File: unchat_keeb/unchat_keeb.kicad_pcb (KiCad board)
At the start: 2 copper layers, 245 parts, among them U1 74HC365, U10 74HC14, U11 74HC14, U12 74HC14, U13 74HC174, U14 74HC174, U15 74HC174, U16 74HC174, U17 74HC174, U18 74HC174, U19 74HC365, U2 74HC365, U20 74HC365, U21 74HC365, U22 74HC365, U23 74HC365, U24 74HC365, U3 74HC365, U4 74HC365, U5 74HC365, U6 74HC365, U7 74HC14, U8 74HC14, U9 74HC14, U99 Raspberry_Pi_Pico

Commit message: Add extra columns, updating to 42-key design
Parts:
- added C37: 0.1uF, Capacitor_SMD:C_0805_2012Metric, F.Cu at (142.8, 142.2)
- added C38: 0.1uF, Capacitor_SMD:C_0805_2012Metric, F.Cu at (142.8, 145.2)
- added C39: 0.1uF, Capacitor_SMD:C_0805_2012Metric, F.Cu at (142.8, 148.2)
- added C40: 0.1uF, Capacitor_SMD:C_0805_2012Metric, F.Cu at (142.8, 151.2)
- added C41: 0.1uF, Capacitor_SMD:C_0805_2012Metric, F.Cu at (142.8, 154.2)
- added C42: 0.1uF, Capacitor_SMD:C_0805_2012Metric, F.Cu at (142.8, 157.2)
- added L1: LED, LED_SMD:LED_0603_1608Metric, F.Cu at (23.7, 133.8)
- added L13: LED, LED_SMD:LED_0603_1608Metric, F.Cu at (23.7, 139.0)
- added L22: LED, LED_SMD:LED_0603_1608Metric, F.Cu at (342.1, 68.9)
- added L28: LED, LED_SMD:LED_0603_1608Metric, F.Cu at (342.1, 71.5)
- added L34: LED, LED_SMD:LED_0603_1608Metric, F.Cu at (342.1, 74.1)
- added L7: LED, LED_SMD:LED_0603_1608Metric, F.Cu at (23.7, 136.4)
- added R103: 100, Resistor_SMD:R_0805_2012Metric, F.Cu at (342.3, 66.1)
- added R117: 68k, Resistor_SMD:R_0805_2012Metric, F.Cu at (147.3, 142.2)
- added R118: 68k, Resistor_SMD:R_0805_2012Metric, F.Cu at (147.3, 145.1)
- added R119: 68k, Resistor_SMD:R_0805_2012Metric, F.Cu at (147.3, 148.1)
- added R120: 68k, Resistor_SMD:R_0805_2012Metric, F.Cu at (147.3, 151.0)
- added R121: 68k, Resistor_SMD:R_0805_2012Metric, F.Cu at (151.7, 142.2)
- added R122: 68k, Resistor_SMD:R_0805_2012Metric, F.Cu at (151.7, 145.1)
- added R123: 1k, Resistor_SMD:R_0805_2012Metric, F.Cu at (151.7, 148.1)
- added R124: 1k, Resistor_SMD:R_0805_2012Metric, F.Cu at (151.7, 151.0)
- added R125: 1k, Resistor_SMD:R_0805_2012Metric, F.Cu at (156.1, 142.2)
- added R126: 1k, Resistor_SMD:R_0805_2012Metric, F.Cu at (156.1, 145.1)
- added R127: 1k, Resistor_SMD:R_0805_2012Metric, F.Cu at (156.1, 148.1)
- added R128: 1k, Resistor_SMD:R_0805_2012Metric, F.Cu at (156.1, 151.0)
- added R73: 100, Resistor_SMD:R_0805_2012Metric, F.Cu at (19.5, 134.0)
- added R79: 100, Resistor_SMD:R_0805_2012Metric, F.Cu at (19.5, 136.9)
- added R85: 100, Resistor_SMD:R_0805_2012Metric, F.Cu at (19.5, 139.9)
- added R91: 100, Resistor_SMD:R_0805_2012Metric, F.Cu at (342.3, 60.2)
- added R97: 100, Resistor_SMD:R_0805_2012Metric, F.Cu at (342.3, 63.2)
- added S1: Keyswitch, GKanwarLibrary:Choc_V1_LED_1.00u, F.Cu at (23.0, 81.3)
- added S13: Keyswitch, GKanwarLibrary:Choc_V1_LED_1.00u, F.Cu at (23.0, 117.5)
- added S22: Keyswitch, GKanwarLibrary:Choc_V1_LED_1.00u, F.Cu at (330.5, 67.8)
- added S28: Keyswitch, GKanwarLibrary:Choc_V1_LED_1.00u, F.Cu at (330.5, 85.9)
- added S34: Keyswitch, GKanwarLibrary:Choc_V1_LED_1.00u, F.Cu at (330.5, 104.0)
- added S7: Keyswitch, GKanwarLibrary:Choc_V1_LED_1.00u, F.Cu at (23.0, 99.4)
- added U25: 74HC14, Package_SO:TSSOP-14_4.4x5mm_P0.65mm, F.Cu at (149.4, 155.8)
- added U26: 74HC174, Package_SO:TSSOP-16_4.4x5mm_P0.65mm, F.Cu at (151.1, 171.6)
- added U27: 74HC365, Package_SO:TSSOP-16_4.4x5mm_P0.65mm, F.Cu at (151.1, 178.2)
- added U66: 74HC365, Package_SO:TSSOP-16_4.4x5mm_P0.65mm, F.Cu at (167.6, 156.2)
- renumbered L8 to L10, L9 to L11, L10 to L12, L11 to L14, L12 to L15, L13 to L16, L14 to L17, L15 to L18, L16 to L19, L1 to L2, L17 to L20, L18 to L21, L19 to L23, L20 to L24, L21 to L25, L22 to L26, L23 to L27, L24 to L29, L2 to L3, L25 to L30, L26 to L31, L27 to L32, L28 to L33, L29 to L35, L30 to L36, L31 to L39, L3 to L4, L32 to L40, L33 to L41, L34 to L42, L35 to L43, L36 to L44, L4 to L5, L5 to L6, L6 to L8, L7 to L9, R98 to R100, R95 to R101, R92 to R102, R107 to R104, R103 to R105, R99 to R106, R96 to R107, R93 to R108, R88 to R111, R89 to R112, R90 to R113, R108 to R114, R104 to R115, R100 to R116, R73 to R74, R74 to R75, R75 to R76, R76 to R77, R77 to R78, R78 to R80, R79 to R81, R80 to R82, R81 to R83, R82 to R84, R83 to R86, R84 to R87, R85 to R88, R86 to R89, R87 to R90, R105 to R92, R101 to R93, R97 to R94, R94 to R95, R91 to R96, R106 to R98, R102 to R99, S8 to S10, S9 to S11, S10 to S12, S11 to S14, S12 to S15, S13 to S16, S14 to S17, S15 to S18, S16 to S19, S1 to S2, S17 to S20, S18 to S21, S19 to S23, S20 to S24, S21 to S25, S22 to S26, S23 to S27, S24 to S29, S2 to S3, S25 to S30, S26 to S31, S27 to S32, S28 to S33, S29 to S35, S30 to S36, S31 to S37, S32 to S38, S33 to S39, S3 to S4, S34 to S40, S35 to S41, S36 to S42, S4 to S5, S5 to S6, S6 to S8, S7 to S9
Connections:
- net /T1 renamed /Left Debounce 1-6/BF6
- net /T10 renamed /Left Debounce 7-12/BF3
- net /T11 renamed /Left Debounce 7-12/BF2
- net /T12 renamed /Left Debounce 7-12/BF1
- net /T13 renamed /Left Debounce 13-18/BF6
- net /T14 renamed /Left Debounce 13-18/BF5
- net /T15 renamed /Left Debounce 13-18/BF4
- net /T16 renamed /Left Debounce 13-18/BF3
- net /T17 renamed /Left Debounce 13-18/BF2
- net /T18 renamed /Left Debounce 13-18/BF1
- net /T19 renamed /Right Debounce 1-7/BF6
- net /T2 renamed /Left Debounce 1-6/BF5
- net /T20 renamed /Right Debounce 1-7/BF5
- net /T21 renamed /Right Debounce 1-7/BF4
- net /T22 renamed /Right Debounce 1-7/BF3
- net /T23 renamed /Right Debounce 1-7/BF2
- net /T24 renamed /Right Debounce 1-7/BF1
- net /T25 renamed /Right Debounce 7-13/BF6
- net /T26 renamed /Right Debounce 7-13/BF5
- net /T27 renamed /Right Debounce 7-13/BF4
- net /T28 renamed /Right Debounce 7-13/BF3
- net /T29 renamed /Right Debounce 7-13/BF2
- net /T3 renamed /Left Debounce 1-6/BF4
- net /T30 renamed /Right Debounce 7-13/BF1
- net /T31 renamed /Right Debounce 13-19/BF6
- net /T32 renamed /Right Debounce 13-19/BF5
- net /T33 renamed /Right Debounce 13-19/BF4
- net /T34 renamed /Right Debounce 13-19/BF3
- net /T35 renamed /Right Debounce 13-19/BF2
- net /T36 renamed /Right Debounce 13-19/BF1
- net /T4 renamed /Left Debounce 1-6/BF3
- net /T5 renamed /Left Debounce 1-6/BF2
- net /T6 renamed /Left Debounce 1-6/BF1
- net /T7 renamed /Left Debounce 7-12/BF6
- net /T8 renamed /Left Debounce 7-12/BF5
- net /T9 renamed /Left Debounce 7-12/BF4
- net /U13_CLK renamed U13_CLK
- net /U14_CLK renamed U14_CLK
- net /U15_CLK renamed U15_CLK
- net /U16_CLK renamed U16_CLK
- net /U17_CLK renamed U17_CLK
- net /U18_CLK renamed U18_CLK
- net /U1_EN renamed U1_EN
- net /U2_EN renamed U2_EN
- net /U3_EN renamed U3_EN
- net /U4_EN renamed U4_EN
- net /U5_EN renamed U5_EN
- net /U6_EN renamed U6_EN
- net EYEL renamed IND1
- net EYER renamed IND2
- L10 pad 1: /LL8 -> /LL10
- L11 pad 1: /LL9 -> /LL11
- L12 pad 1: /LL10 -> /LL12
- L14 pad 1: /LL11 -> /LL14
- L15 pad 1: /LL12 -> /LL15
- L16 pad 1: /LL13 -> /LL16
- L17 pad 1: /LL14 -> /LL17
- L18 pad 1: /LL15 -> /LL18
- L19 pad 1: /LL16 -> /LL19
- L2 pad 1: /LL1 -> /LL2
- L20 pad 1: /LL17 -> /LL20
- L21 pad 1: /LL18 -> /LL21
- L23 pad 1: /LR1 -> /LR2
- L24 pad 1: /LR2 -> /LR3
- L25 pad 1: /LR3 -> /LR4
- L26 pad 1: /LR4 -> /LR5
- L27 pad 1: /LR5 -> /LR6
- L29 pad 1: /LR6 -> /LR8
- L3 pad 1: /LL2 -> /LL3
- L30 pad 1: /LR7 -> /LR9
- L31 pad 1: /LR8 -> /LR10
- L32 pad 1: /LR9 -> /LR11
- L33 pad 1: /LR10 -> /LR12
- L35 pad 1: /LR11 -> /LR14
- L36 pad 1: /LR12 -> /LR15
- L39 pad 1: /LR13 -> /LR16
- L4 pad 1: /LL3 -> /LL4
- L40 pad 1: /LR14 -> /LR17
- L41 pad 1: /LR15 -> /LR18
- L42 pad 1: /LR16 -> /LR19
- L43 pad 1: /LR17 -> /LR20
- L44 pad 1: /LR18 -> /LR21
- L5 pad 1: /LL4 -> /LL5
- L6 pad 1: /LL5 -> /LL6
- L8 pad 1: /LL6 -> /LL8
- L9 pad 1: /LL7 -> /LL9
- R37 pad 1: /S19a -> /S22a
- R38 pad 1: /S19a -> /S22a
- R39 pad 1: /S20a -> /S23a
- R40 pad 1: /S20a -> /S23a
- R41 pad 1: /S21a -> /S24a
- R42 pad 1: /S21a -> /S24a
- R43 pad 1: /S22a -> /S25a
- R44 pad 1: /S22a -> /S25a
- R45 pad 1: /S23a -> /S26a
- R46 pad 1: /S23a -> /S26a
- R47 pad 1: /S24a -> /S27a
- R48 pad 1: /S24a -> /S27a
- R49 pad 1: /S25a -> /S28a
- R50 pad 1: /S25a -> /S28a
- R51 pad 1: /S26a -> /S29a
- R52 pad 1: /S26a -> /S29a
- R53 pad 1: /S27a -> /S30a
- R54 pad 1: /S27a -> /S30a
- R55 pad 1: /S28a -> /S31a
- R56 pad 1: /S28a -> /S31a
- R57 pad 1: /S29a -> /S32a
- R58 pad 1: /S29a -> /S32a
- R59 pad 1: /S30a -> /S33a
- R60 pad 1: /S30a -> /S33a
- R61 pad 1: /S31a -> /S34a
- R62 pad 1: /S31a -> /S34a
- R63 pad 1: /S32a -> /S35a
- R64 pad 1: /S32a -> /S35a
- R65 pad 1: /S33a -> /S36a
- R66 pad 1: /S33a -> /S36a
- R67 pad 1: /S34a -> /S37a
- R68 pad 1: /S34a -> /S37a
- R69 pad 1: /S35a -> /S38a
- R70 pad 1: /S35a -> /S38a
- R71 pad 1: /S36a -> /S39a
- R72 pad 1: /S36a -> /S39a
- S10 pad 1: /S8a -> /S10a
- S11 pad 1: /S9a -> /S11a
- S12 pad 1: /S10a -> /S12a
- S14 pad 1: /S11a -> /S14a
- S15 pad 1: /S12a -> /S15a
- S16 pad 1: /S13a -> /S16a
- S17 pad 1: /S14a -> /S17a
- S18 pad 1: /S15a -> /S18a
- S19 pad 1: /S16a -> /S19a
- S2 pad 1: /S1a -> /S2a
- S20 pad 1: /S17a -> /S20a
- S21 pad 1: /S18a -> /S21a
- S23 pad 1: /S19a -> /S23a
- S24 pad 1: /S20a -> /S24a
- S25 pad 1: /S21a -> /S25a
- S26 pad 1: /S22a -> /S26a
- S27 pad 1: /S23a -> /S27a
- S29 pad 1: /S24a -> /S29a
- S3 pad 1: /S2a -> /S3a
- S30 pad 1: /S25a -> /S30a
- S31 pad 1: /S26a -> /S31a
- S32 pad 1: /S27a -> /S32a
- S33 pad 1: /S28a -> /S33a
- S35 pad 1: /S29a -> /S35a
- S36 pad 1: /S30a -> /S36a
- S37 pad 1: /S31a -> /S37a
- S38 pad 1: /S32a -> /S38a
- S39 pad 1: /S33a -> /S39a
- S4 pad 1: /S3a -> /S4a
- S40 pad 1: /S34a -> /S40a
- S41 pad 1: /S35a -> /S41a
- S42 pad 1: /S36a -> /S42a
- S5 pad 1: /S4a -> /S5a
- S6 pad 1: /S5a -> /S6a
- S8 pad 1: /S6a -> /S8a
- S9 pad 1: /S7a -> /S9a
- U13 pad 1: /LED_RST -> LED_RST
- U14 pad 1: /LED_RST -> LED_RST
- U15 pad 1: /LED_RST -> LED_RST
- U16 pad 1: /LED_RST -> LED_RST
- U17 pad 1: /LED_RST -> LED_RST
- U18 pad 1: /LED_RST -> LED_RST
- U19 pad 1: /LED_DIM -> LED_DIM
- U19 pad 15: /LED_DIM -> LED_DIM
- U20 pad 1: /LED_DIM -> LED_DIM
- U20 pad 15: /LED_DIM -> LED_DIM
- U21 pad 1: /LED_DIM -> LED_DIM
- U21 pad 15: /LED_DIM -> LED_DIM
- U22 pad 1: /LED_DIM -> LED_DIM
- U22 pad 15: /LED_DIM -> LED_DIM
- U23 pad 1: /LED_DIM -> LED_DIM
- U23 pad 15: /LED_DIM -> LED_DIM
- U24 pad 1: /LED_DIM -> LED_DIM
- U24 pad 15: /LED_DIM -> LED_DIM
- U99 pad 19: /LED_RST -> U66_EN
- U99 pad 20: /LED_DIM -> U26_CLK
- U99 pad 31: unconnected-(U99-GPIO26_ADC0-Pad31) -> LED_DIM
- U99 pad 32: unconnected-(U99-GPIO27_ADC1-Pad32) -> LED_RST
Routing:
- net /S32a: track 5.84 -> 0.00 mm
- net /S35a: track 5.66 -> 11.5 mm
- net /S34a: track 5.70 -> 11.5 mm
- net /S31a: track 5.84 -> 0.00 mm
- net /S36a: track 0.00 -> 5.84 mm
- net /S33a: track 5.84 -> 0.00 mm
- net /S29a: track 5.84 -> 8.84 mm
- net /S26a: track 3.00 -> 0.00 mm

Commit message: Add dxf layout and finish half keyboard pbc layout
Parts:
- C37, C38, C39, C40, C41, C42, R103, R117, R118, R119, R120, R121, R122, R123, R124, R125, R126, R127, R128, R73, R79, R85, R91, R97, U26, U27: moved to B.Cu
- U1, U13, U14, U15, U2, U3: moved to F.Cu
- U99: footprint ScottoKeebs_MCU:Raspberry_Pi_Pico -> ScottoKeebs_MCU:Raspberry_Pi_Pico_SMD
- moved U10 233.7 mm to (122.5, 231.5)
- moved U4 233.7 mm to (116.5, 231.5)
- moved L34 213.5 mm to (260.0, 271.2)
- moved L28 199.3 mm to (260.0, 253.1)
- moved L22 185.3 mm to (260.0, 235.0)
- moved L42 177.1 mm to (191.5, 276.5)
- moved C19 177.1 mm to (235.5, 223.5)
- moved C20 177.1 mm to (217.5, 209.5)
- moved C21 177.1 mm to (199.5, 202.5)
- moved C22 177.1 mm to (181.5, 209.5)
- moved C23 177.1 mm to (163.5, 212.5)
- moved C24 177.1 mm to (235.5, 240.5)
- moved C25 177.1 mm to (217.5, 226.5)
- moved C26 177.1 mm to (199.5, 219.5)
- moved C27 177.1 mm to (181.5, 226.5)
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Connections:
- U10 pad 1: /Right Debounce 1-7/Db1 -> /Right Debounce 1-7/Db4
- U10 pad 11: /Right Debounce 1-7/Db5 -> /Right Debounce 1-7/Db2
- U10 pad 13: /Right Debounce 1-7/Db6 -> /Right Debounce 1-7/Db3
- U10 pad 3: /Right Debounce 1-7/Db2 -> /Right Debounce 1-7/Db5
- U10 pad 5: /Right Debounce 1-7/Db3 -> /Right Debounce 1-7/Db6
- U10 pad 9: /Right Debounce 1-7/Db4 -> /Right Debounce 1-7/Db1
- U11 pad 1: /Right Debounce 7-13/Db1 -> /Right Debounce 7-13/Db4
- U11 pad 11: /Right Debounce 7-13/Db5 -> /Right Debounce 7-13/Db2
- U11 pad 13: /Right Debounce 7-13/Db6 -> /Right Debounce 7-13/Db3
- U11 pad 3: /Right Debounce 7-13/Db2 -> /Right Debounce 7-13/Db5
- U11 pad 5: /Right Debounce 7-13/Db3 -> /Right Debounce 7-13/Db6
- U11 pad 9: /Right Debounce 7-13/Db4 -> /Right Debounce 7-13/Db1
- U12 pad 1: /Right Debounce 13-19/Db1 -> /Right Debounce 13-19/Db4
- U12 pad 11: /Right Debounce 13-19/Db5 -> /Right Debounce 13-19/Db2
- U12 pad 13: /Right Debounce 13-19/Db6 -> /Right Debounce 13-19/Db3
- U12 pad 3: /Right Debounce 13-19/Db2 -> /Right Debounce 13-19/Db5
- U12 pad 5: /Right Debounce 13-19/Db3 -> /Right Debounce 13-19/Db6
- U12 pad 9: /Right Debounce 13-19/Db4 -> /Right Debounce 13-19/Db1
- U13 pad 11: /BUS4 -> /BUS6
- U13 pad 14: /BUS6 -> /BUS4
- U13 pad 3: /BUS1 -> /BUS3
- U13 pad 6: /BUS3 -> /BUS1
- U14 pad 11: /BUS4 -> /BUS6
- U14 pad 14: /BUS6 -> /BUS4
- U14 pad 3: /BUS1 -> /BUS3
- U14 pad 6: /BUS3 -> /BUS1
- U15 pad 11: /BUS4 -> /BUS6
- U15 pad 14: /BUS6 -> /BUS4
- U15 pad 3: /BUS1 -> /BUS3
- U15 pad 6: /BUS3 -> /BUS1
- U16 pad 11: /BUS4 -> /BUS6
- U16 pad 14: /BUS6 -> /BUS4
- U16 pad 3: /BUS1 -> /BUS3
- U16 pad 6: /BUS3 -> /BUS1
- U17 pad 11: /BUS4 -> /BUS6
- U17 pad 14: /BUS6 -> /BUS4
- U17 pad 3: /BUS1 -> /BUS3
- U17 pad 6: /BUS3 -> /BUS1
- U18 pad 11: /BUS4 -> /BUS6
- U18 pad 14: /BUS6 -> /BUS4
- U18 pad 3: /BUS1 -> /BUS3
- U18 pad 6: /BUS3 -> /BUS1
- U19 pad 10: /Left LED Control 1-6/Q5 -> /Left LED Control 1-6/Q2
- U19 pad 12: /Left LED Control 1-6/Q4 -> /Left LED Control 1-6/Q1
- U19 pad 14: /Left LED Control 1-6/Q3 -> /Left LED Control 1-6/Q0
- U19 pad 2: /Left LED Control 1-6/Q2 -> /Left LED Control 1-6/Q5
- U19 pad 4: /Left LED Control 1-6/Q1 -> /Left LED Control 1-6/Q4
- U19 pad 6: /Left LED Control 1-6/Q0 -> /Left LED Control 1-6/Q3
- U20 pad 10: /Left LED Control 7-12/Q5 -> /Left LED Control 7-12/Q2
- U20 pad 12: /Left LED Control 7-12/Q4 -> /Left LED Control 7-12/Q1
- U20 pad 14: /Left LED Control 7-12/Q3 -> /Left LED Control 7-12/Q0
- U20 pad 2: /Left LED Control 7-12/Q2 -> /Left LED Control 7-12/Q5
- U20 pad 4: /Left LED Control 7-12/Q1 -> /Left LED Control 7-12/Q4
- U20 pad 6: /Left LED Control 7-12/Q0 -> /Left LED Control 7-12/Q3
- U21 pad 10: /Left LED Control 13-18/Q5 -> /Left LED Control 13-18/Q2
- U21 pad 12: /Left LED Control 13-18/Q4 -> /Left LED Control 13-18/Q1
- U21 pad 14: /Left LED Control 13-18/Q3 -> /Left LED Control 13-18/Q0
- U21 pad 2: /Left LED Control 13-18/Q2 -> /Left LED Control 13-18/Q5
- U21 pad 4: /Left LED Control 13-18/Q1 -> /Left LED Control 13-18/Q4
- U21 pad 6: /Left LED Control 13-18/Q0 -> /Left LED Control 13-18/Q3
- U22 pad 10: /Right LED Control 1-6/Q5 -> /Right LED Control 1-6/Q2
- U22 pad 12: /Right LED Control 1-6/Q4 -> /Right LED Control 1-6/Q1
- U22 pad 14: /Right LED Control 1-6/Q3 -> /Right LED Control 1-6/Q0
- U22 pad 2: /Right LED Control 1-6/Q2 -> /Right LED Control 1-6/Q5
- U22 pad 4: /Right LED Control 1-6/Q1 -> /Right LED Control 1-6/Q4
- U22 pad 6: /Right LED Control 1-6/Q0 -> /Right LED Control 1-6/Q3
- U23 pad 10: /Right LED Control 7-12/Q5 -> /Right LED Control 7-12/Q2
- U23 pad 12: /Right LED Control 7-12/Q4 -> /Right LED Control 7-12/Q1
- U23 pad 14: /Right LED Control 7-12/Q3 -> /Right LED Control 7-12/Q0
- U23 pad 2: /Right LED Control 7-12/Q2 -> /Right LED Control 7-12/Q5
- U23 pad 4: /Right LED Control 7-12/Q1 -> /Right LED Control 7-12/Q4
- U23 pad 6: /Right LED Control 7-12/Q0 -> /Right LED Control 7-12/Q3
- U24 pad 10: /Right LED Control 13-18/Q5 -> /Right LED Control 13-18/Q2
- U24 pad 12: /Right LED Control 13-18/Q4 -> /Right LED Control 13-18/Q1
- U24 pad 14: /Right LED Control 13-18/Q3 -> /Right LED Control 13-18/Q0
- U24 pad 2: /Right LED Control 13-18/Q2 -> /Right LED Control 13-18/Q5
- U24 pad 4: /Right LED Control 13-18/Q1 -> /Right LED Control 13-18/Q4
- U24 pad 6: /Right LED Control 13-18/Q0 -> /Right LED Control 13-18/Q3
- U25 pad 1: /Thumb Debounce/Db1 -> /Thumb Debounce/Db4
- U25 pad 11: /Thumb Debounce/Db5 -> /Thumb Debounce/Db2
- U25 pad 13: /Thumb Debounce/Db6 -> /Thumb Debounce/Db3
- U25 pad 3: /Thumb Debounce/Db2 -> /Thumb Debounce/Db5
- U25 pad 5: /Thumb Debounce/Db3 -> /Thumb Debounce/Db6
- U25 pad 9: /Thumb Debounce/Db4 -> /Thumb Debounce/Db1
- U26 pad 11: /BUS4 -> /BUS6
- U26 pad 14: /BUS6 -> /BUS4
- U26 pad 3: /BUS1 -> /BUS3
- U26 pad 6: /BUS3 -> /BUS1
- U27 pad 10: /Thumb LED Control/Q5 -> /Thumb LED Control/Q2
- U27 pad 12: /Thumb LED Control/Q4 -> /Thumb LED Control/Q1
- U27 pad 14: /Thumb LED Control/Q3 -> /Thumb LED Control/Q0
- U27 pad 2: /Thumb LED Control/Q2 -> /Thumb LED Control/Q5
- U27 pad 4: /Thumb LED Control/Q1 -> /Thumb LED Control/Q4
- U27 pad 6: /Thumb LED Control/Q0 -> /Thumb LED Control/Q3
- U7 pad 1: /Left Debounce 1-6/Db1 -> /Left Debounce 1-6/Db4
- U7 pad 11: /Left Debounce 1-6/Db5 -> /Left Debounce 1-6/Db2
- U7 pad 13: /Left Debounce 1-6/Db6 -> /Left Debounce 1-6/Db3
- U7 pad 3: /Left Debounce 1-6/Db2 -> /Left Debounce 1-6/Db5
- U7 pad 5: /Left Debounce 1-6/Db3 -> /Left Debounce 1-6/Db6
- U7 pad 9: /Left Debounce 1-6/Db4 -> /Left Debounce 1-6/Db1
- U8 pad 1: /Left Debounce 7-12/Db1 -> /Left Debounce 7-12/Db4
- U8 pad 11: /Left Debounce 7-12/Db5 -> /Left Debounce 7-12/Db2
- U8 pad 13: /Left Debounce 7-12/Db6 -> /Left Debounce 7-12/Db3
- U8 pad 3: /Left Debounce 7-12/Db2 -> /Left Debounce 7-12/Db5
- U8 pad 5: /Left Debounce 7-12/Db3 -> /Left Debounce 7-12/Db6
- U8 pad 9: /Left Debounce 7-12/Db4 -> /Left Debounce 7-12/Db1
- U9 pad 1: /Left Debounce 13-18/Db1 -> /Left Debounce 13-18/Db4
- U9 pad 11: /Left Debounce 13-18/Db5 -> /Left Debounce 13-18/Db2
- U9 pad 13: /Left Debounce 13-18/Db6 -> /Left Debounce 13-18/Db3
- U9 pad 3: /Left Debounce 13-18/Db2 -> /Left Debounce 13-18/Db5
- U9 pad 5: /Left Debounce 13-18/Db3 -> /Left Debounce 13-18/Db6
- U9 pad 9: /Left Debounce 13-18/Db4 -> /Left Debounce 13-18/Db1
- U99 pad 10: IND2 -> U13_CLK
- U99 pad 11: U1_EN -> U2_EN
- U99 pad 12: U2_EN -> U14_CLK
- U99 pad 14: U3_EN -> IND1
- U99 pad 15: U13_CLK -> IND2
- U99 pad 16: U14_CLK -> U3_EN
- U99 pad 22: U17_CLK -> U6_EN
- U99 pad 24: U16_CLK -> U17_CLK
- U99 pad 25: U6_EN -> U5_EN
- U99 pad 26: U5_EN -> U16_CLK
- U99 pad 9: IND1 -> U1_EN
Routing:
- net LED_DIM: track 0.00 -> 137.2 mm, vias 0 -> 9
- net /BUS3: track 0.00 -> 128.7 mm, vias 0 -> 6
- net /LL13: track 0.00 -> 125.5 mm, vias 0 -> 1
- net /BUS2: track 0.00 -> 120.1 mm, vias 0 -> 6
- net /LL7: track 0.00 -> 119.0 mm, vias 0 -> 1
- net /Left Debounce 1-6/Db1: track 2.52 -> 121.3 mm
- net /Left Debounce 7-12/Db1: track 2.52 -> 118.3 mm
- net /LL1: track 0.00 -> 115.1 mm, vias 0 -> 1
- net /BUS4: track 0.00 -> 114.8 mm, vias 0 -> 2
- net /BUS1: track 0.00 -> 114.4 mm, vias 0 -> 6
- net /Left Debounce 13-18/Db1: track 2.52 -> 111.5 mm
- net LED_RST: track 0.00 -> 105.9 mm, vias 0 -> 4
- net /BUS5: track 0.00 -> 105.9 mm, vias 0 -> 2
- net /LL14: track 0.00 -> 105.4 mm, vias 0 -> 1
- net /Left Debounce 1-6/Db2: track 2.52 -> 103.5 mm
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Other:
- board outline added: 274 x 102 mm

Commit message: Position right switches, update dxf dims, and fix symb lib paths
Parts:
- U16, U17, U18, U4, U5, U6: moved to F.Cu
- moved R120 234.5 mm to (266.1, 104.1), turned to -165 degrees
- moved R126 226.8 mm to (266.6, 106.0), turned to -165 degrees
- moved C40 224.8 mm to (267.1, 107.9), turned to 15 degrees
- moved R121 209.2 mm to (248.9, 117.5), turned to -150 degrees
- moved C33 202.7 mm to (284.5, 83.9), turned to 15 degrees
- moved C41 202.5 mm to (250.9, 121.0), turned to 30 degrees
- moved R66 201.5 mm to (284.0, 82.0), turned to -165 degrees
- moved R127 201.3 mm to (249.9, 119.2), turned to -150 degrees
- moved R65 200.3 mm to (283.5, 80.0), turned to -165 degrees
- moved C36 199.4 mm to (232.5, 98.4), turned to 15 degrees
- moved C32 198.4 mm to (304.1, 87.5), turned to 15 degrees
- moved R72 198.2 mm to (231.9, 96.4), turned to -165 degrees
- moved C34 197.4 mm to (267.1, 88.6), turned to 15 degrees
- moved R64 197.3 mm to (303.6, 85.5), turned to -165 degrees
- moved R71 197.0 mm to (231.4, 94.5), turned to -165 degrees
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
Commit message: Route remaining components, except VCC and GND
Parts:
- U25: moved to B.Cu
- U26: moved to F.Cu
- moved U27 70.6 mm to (218.5, 132.5), turned to 0 degrees
- moved U26 64.8 mm to (218.5, 132.5), turned to 180 degrees
- moved U25 35.3 mm to (181.5, 132.5), turned to 180 degrees
- moved U66 30.0 mm to (181.5, 132.5), turned to 180 degrees
- moved R98 0.97 mm to (309.2, 76.6)
- moved R104 0.89 mm to (313.6, 93.1)
- moved R93 0.89 mm to (285.2, 56.7)
- moved R101 0.89 mm to (254.9, 82.4)
- moved R106 0.89 mm to (276.7, 94.2)
- moved R92 0.89 mm to (304.8, 60.2)
- moved R95 0.89 mm to (250.5, 66.0)
- moved R100 0.89 mm to (272.3, 77.7)
- moved R108 0.89 mm to (241.9, 103.5)
- moved R105 0.89 mm to (294.0, 89.5)
- moved R94 0.89 mm to (267.9, 61.3)
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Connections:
- U99 pad 33: unconnected-(U99-AGND-Pad33) -> GND
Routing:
- net /BUS6: track 93.6 -> 282.5 mm, vias 2 -> 8
- net /BUS5: track 105.9 -> 288.7 mm, vias 2 -> 8
- net /BUS4: track 114.8 -> 286.5 mm, vias 2 -> 8
- net /BUS1: track 114.4 -> 273.7 mm, vias 6 -> 15
- net /BUS3: track 128.7 -> 284.3 mm, vias 6 -> 15
- net /BUS2: track 120.1 -> 274.3 mm, vias 6 -> 15
- net /LR13: track 0.00 -> 116.2 mm, vias 0 -> 1
- net /Right Debounce 13-19/Db1: track 0.00 -> 115.6 mm, vias 0 -> 2
- net LED_DIM: track 137.2 -> 247.5 mm, vias 9 -> 14
- net /LR7: track 0.00 -> 109.9 mm, vias 0 -> 1
- net /Right Debounce 1-7/Db1: track 0.00 -> 109.7 mm, vias 0 -> 2
- net /Right Debounce 7-13/Db1: track 0.00 -> 108.1 mm, vias 0 -> 2
- net /Thumb Debounce/Db4: track 0.00 -> 106.9 mm, vias 0 -> 2
- net /LR1: track 0.00 -> 106.1 mm, vias 0 -> 1
- net /LL19: track 0.00 -> 102.5 mm, vias 0 -> 1
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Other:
- outline, holes or cut-outs redrawn
- board text added: "JLCJLCJLCJLC"

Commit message: Finalize the board
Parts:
- added C43: 0.1uF, Capacitor_SMD:C_0805_2012Metric, B.Cu at (175.0, 128.0)
- added C44: 0.1uF, Capacitor_SMD:C_0805_2012Metric, B.Cu at (172.0, 122.0)
- added C45: 0.1uF, Capacitor_SMD:C_0805_2012Metric, B.Cu at (198.5, 91.5)
- added C46: 0.1uF, Capacitor_SMD:C_0805_2012Metric, B.Cu at (176.0, 66.5)
- added C47: 0.1uF, Capacitor_SMD:C_0805_2012Metric, B.Cu at (218.5, 76.0)
- added C48: 0.1uF, Capacitor_SMD:C_0805_2012Metric, B.Cu at (206.5, 92.0)
- added C49: 0.1uF, Capacitor_SMD:C_0805_2012Metric, B.Cu at (206.5, 114.5)
- added C50: 0.1uF, Capacitor_SMD:C_0805_2012Metric, B.Cu at (226.0, 128.0)
- U1, U13, U14, U15, U16, U17, U18, U19, U2, U20, U21, U22, U23, U24, U26, U27, U3, U4, U5, U6, U66: footprint Package_SO:TSSOP-16_4.4x5mm_P0.65mm -> GKanwarLibrary:TSSOP-16_4.4x5mm_P0.65mm
- U10, U11, U12, U25, U7, U8, U9: footprint Package_SO:TSSOP-14_4.4x5mm_P0.65mm -> GKanwarLibrary:TSSOP-14_4.4x5mm_P0.65mm
- moved C40 0.19 mm to (267.4, 108.0)
- moved R120 0.19 mm to (266.4, 104.2)
- moved R126 0.19 mm to (266.9, 106.1)
- moved R21 0.09 mm to (149.7, 71.2)
- moved C11 0.09 mm to (148.7, 75.1)
- moved R22 0.09 mm to (149.2, 73.1)
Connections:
- U99 pad 42: unconnected-(U99-GND-Pad42) -> GND
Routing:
- net VCC: track 0.00 -> 211.4 mm, vias 0 -> 70
- net GND: track 3.18 -> 212.3 mm, vias 2 -> 76
- net U2_EN: track 21.5 -> 16.8 mm
- net U4_EN: track 52.9 -> 57.2 mm
- net /BUS1: track 273.7 -> 270.1 mm, vias 15 -> 14
- net VBUS: track 0.00 -> 2.54 mm
- net U66_EN: track 26.7 -> 29.2 mm
- net U13_CLK: track 26.4 -> 23.8 mm
- net /Right Debounce 7-13/Db1: track 108.1 -> 106.1 mm
- net U16_CLK: track 37.9 -> 35.9 mm
- net /Left Debounce 7-12/Db4: track 67.3 -> 65.6 mm
- net U5_EN: track 35.6 -> 33.9 mm, vias 0 -> 2
- net U17_CLK: track 21.6 -> 20.0 mm
- net LED_RST: track 175.5 -> 177.1 mm
- net /BUS6: track 282.5 -> 281.0 mm
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- added copper zone on B.Cu, net GND
- added copper zone on F.Cu, net VCC
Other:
- outline, holes or cut-outs redrawn
- board text added: "UnChat-42"
- board text added: "by Tej Kanwar"

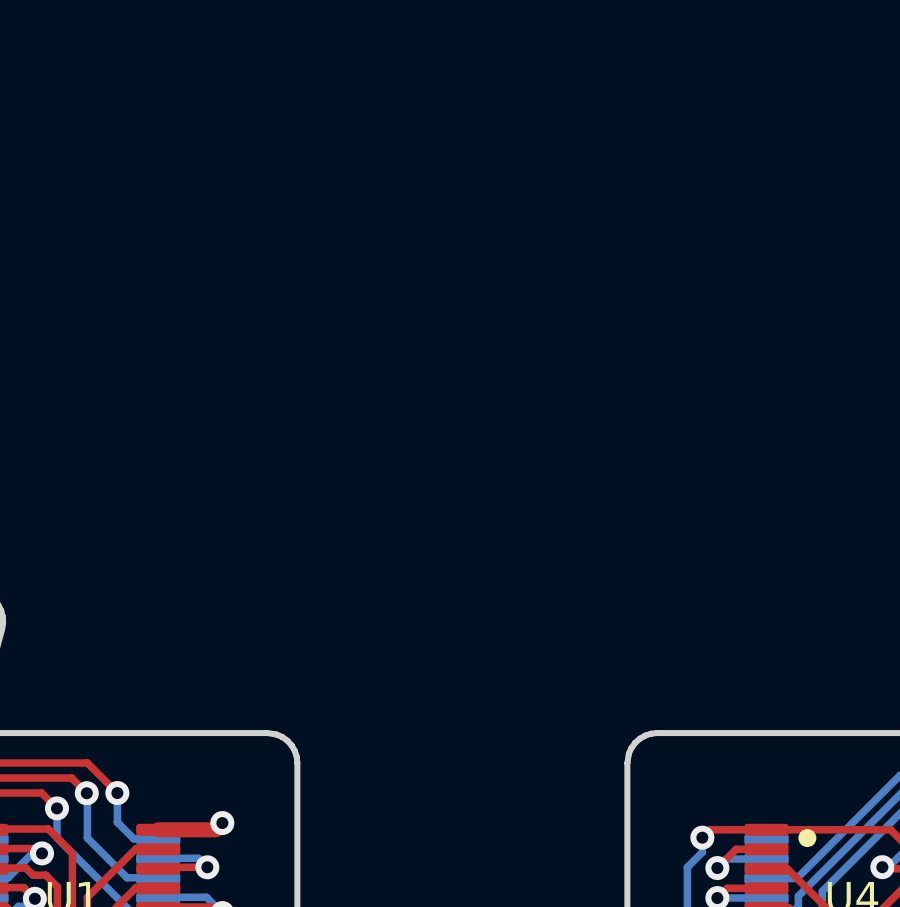
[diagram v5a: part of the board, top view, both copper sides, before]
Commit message: Add bus pullups, still need to route 'em
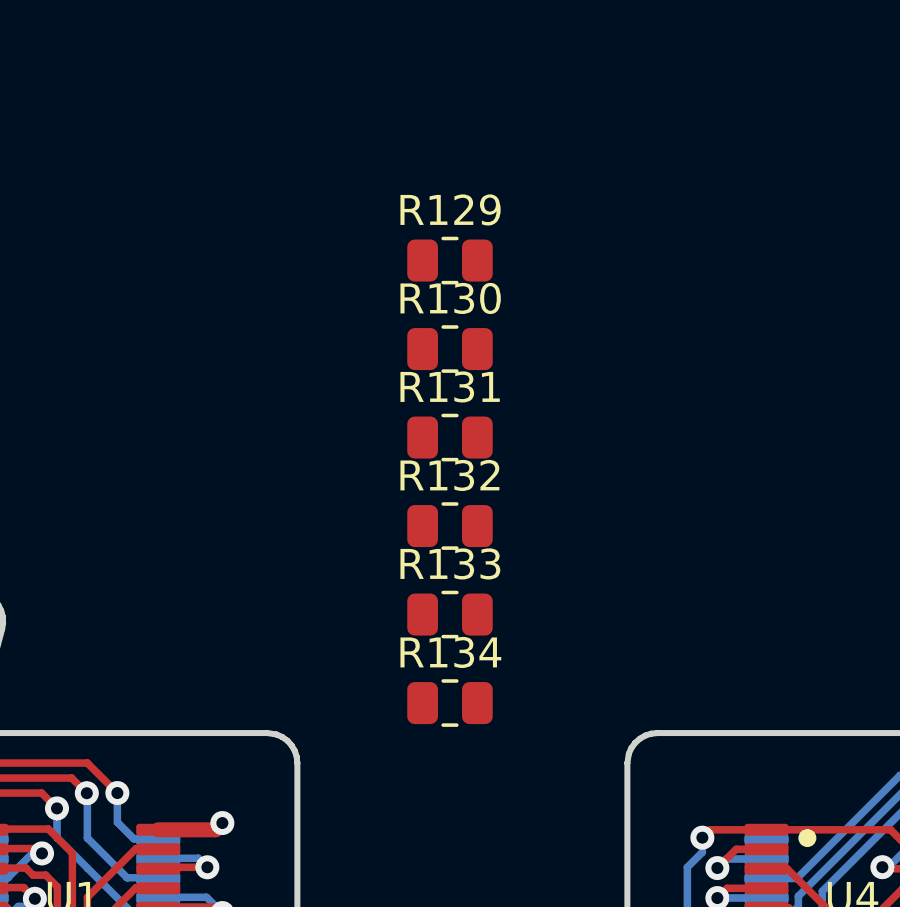
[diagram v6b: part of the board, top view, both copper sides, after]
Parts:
- added R129: 1k, Resistor_SMD:R_0805_2012Metric, F.Cu at (199.6, 49.2)
- added R130: 1k, Resistor_SMD:R_0805_2012Metric, F.Cu at (199.6, 52.2)
- added R131: 1k, Resistor_SMD:R_0805_2012Metric, F.Cu at (199.6, 55.1)
- added R132: 1k, Resistor_SMD:R_0805_2012Metric, F.Cu at (199.6, 58.1)
- added R133: 1k, Resistor_SMD:R_0805_2012Metric, F.Cu at (199.6, 61.0)
- added R134: 1k, Resistor_SMD:R_0805_2012Metric, F.Cu at (199.6, 64.0)
